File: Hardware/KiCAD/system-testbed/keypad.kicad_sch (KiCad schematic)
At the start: 43 parts, among them J6 HW-834 Module, SW10 *, SW11 2, SW12 5, SW13 8, SW14 0, SW15 3, SW16 6, SW17 9, SW18 #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

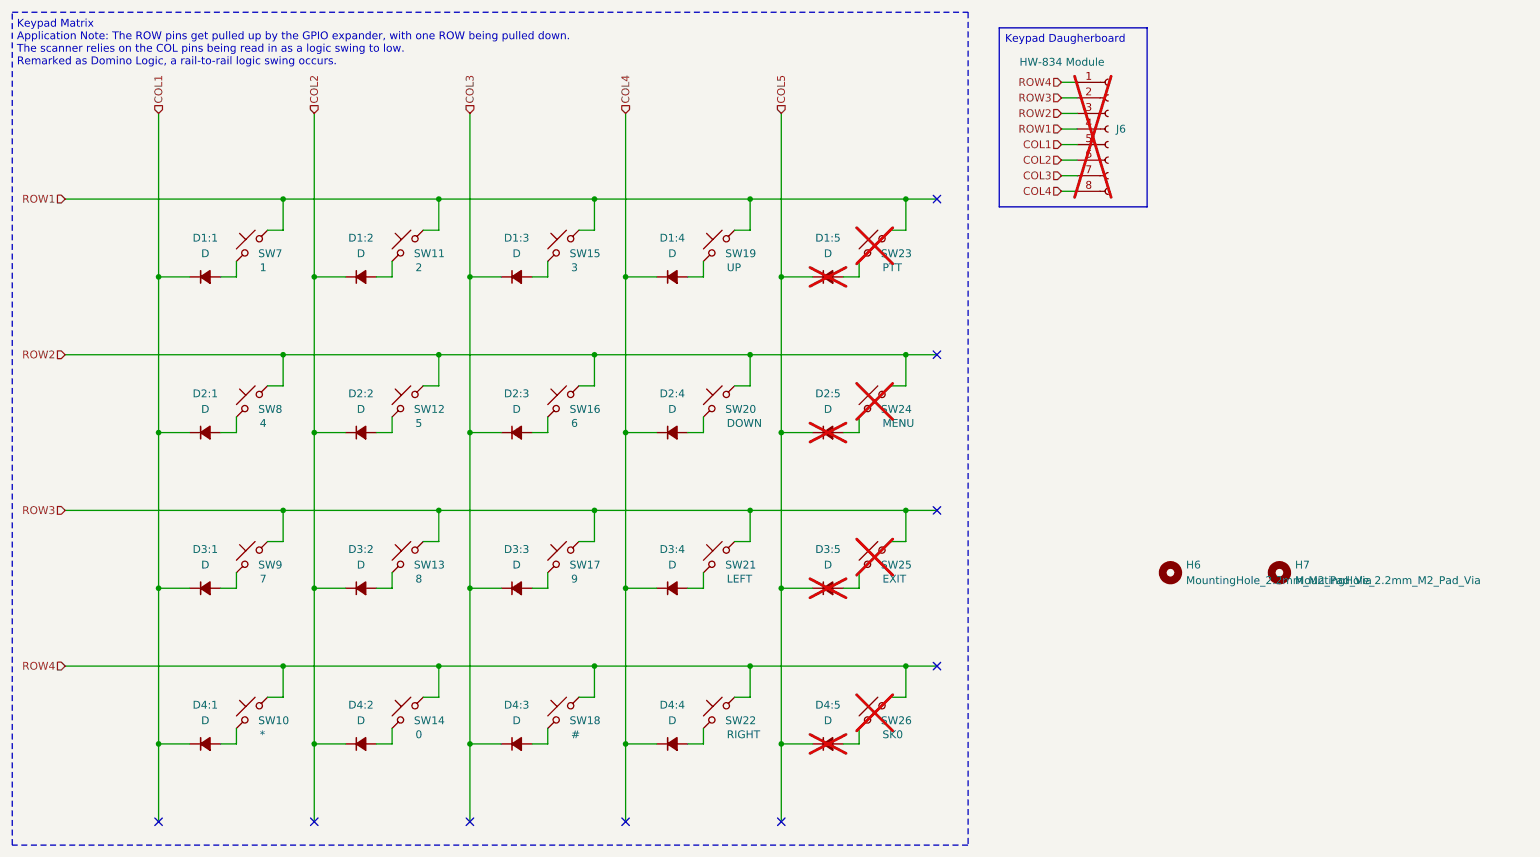
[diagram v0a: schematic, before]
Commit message: fix: remove unused mounting holes for HW #69 fix: edit symbol fields of button matrix #69
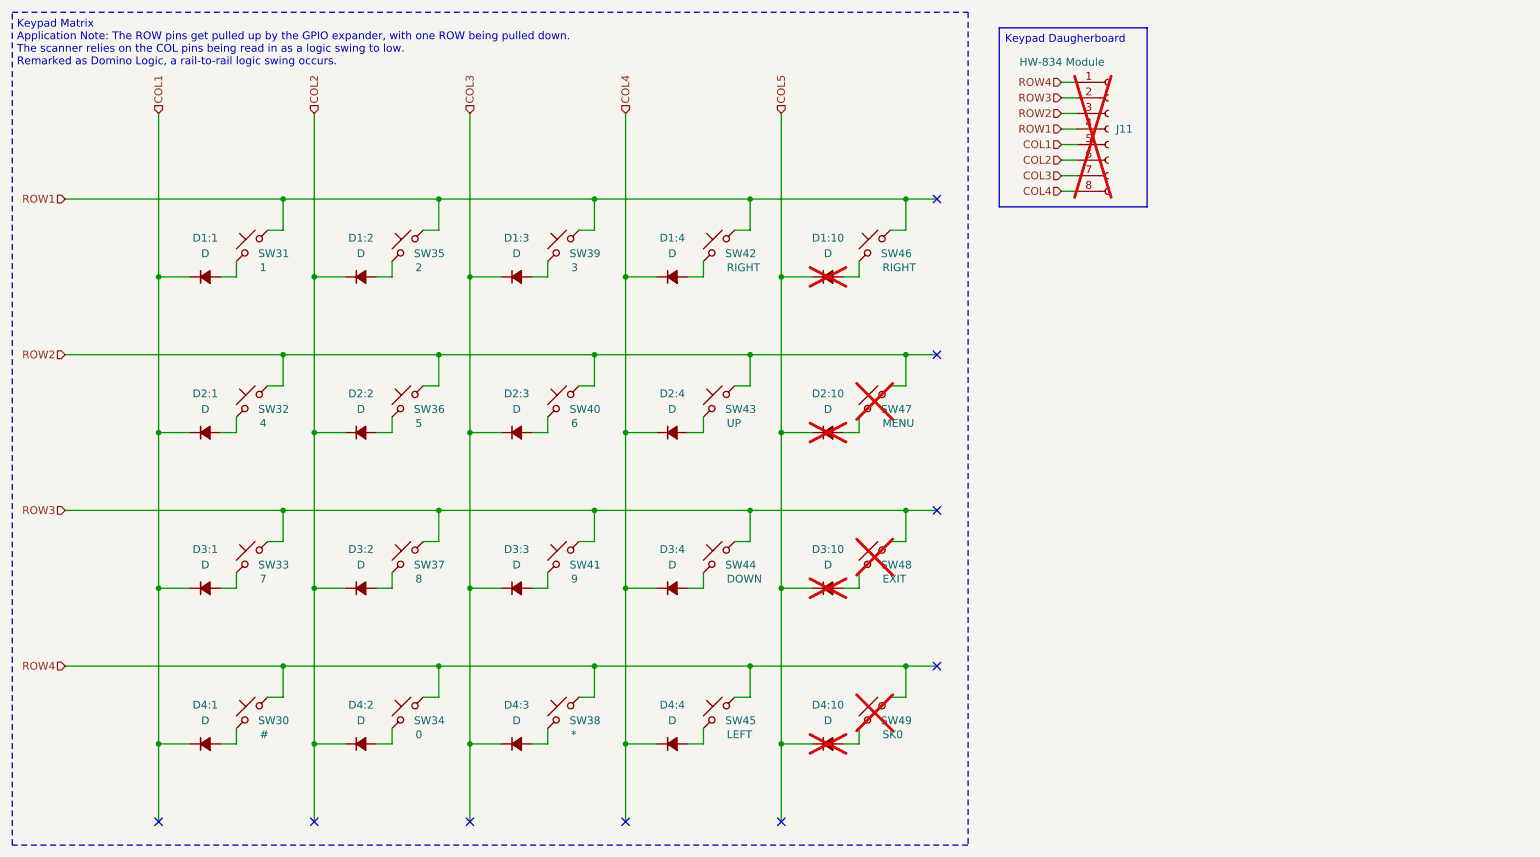
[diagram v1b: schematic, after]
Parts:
- removed H6: MountingHole_2.2mm_M2_Pad_Via, MountingHole:MountingHole_2.2mm_M2_Pad_Via, symbol Mechanical:MountingHole
- removed H7: MountingHole_2.2mm_M2_Pad_Via, MountingHole:MountingHole_6.4mm_M6_Pad_Via, symbol Mechanical:MountingHole
- SW30: renamed from SW7; value 1 -> #; footprint Button_Switch_THT:SW_PUSH_6mm_H7.3mm -> Button_Switch_SMD:SW_Push_1P1T_NO_CK_KMR2
- SW31: renamed from SW8; value 4 -> 1; footprint Button_Switch_THT:SW_PUSH_6mm_H7.3mm -> Button_Switch_SMD:SW_Push_1P1T_NO_CK_KMR2
- SW32: renamed from SW9; value 7 -> 4; footprint Button_Switch_THT:SW_PUSH_6mm_H7.3mm -> Button_Switch_SMD:SW_Push_1P1T_NO_CK_KMR2
- SW33: renamed from SW10; value * -> 7; footprint Button_Switch_THT:SW_PUSH_6mm_H7.3mm -> Button_Switch_SMD:SW_Push_1P1T_NO_CK_KMR2
- SW34: renamed from SW11; value 2 -> 0; footprint Button_Switch_THT:SW_PUSH_6mm_H7.3mm -> Button_Switch_SMD:SW_Push_1P1T_NO_CK_KMR2
- SW35: renamed from SW12; value 5 -> 2; footprint Button_Switch_THT:SW_PUSH_6mm_H7.3mm -> Button_Switch_SMD:SW_Push_1P1T_NO_CK_KMR2
- SW36: renamed from SW13; value 8 -> 5; footprint Button_Switch_THT:SW_PUSH_6mm_H7.3mm -> Button_Switch_SMD:SW_Push_1P1T_NO_CK_KMR2
- SW37: renamed from SW14; value 0 -> 8; footprint Button_Switch_THT:SW_PUSH_6mm_H7.3mm -> Button_Switch_SMD:SW_Push_1P1T_NO_CK_KMR2
- SW38: renamed from SW15; value 3 -> *; footprint Button_Switch_THT:SW_PUSH_6mm_H7.3mm -> Button_Switch_SMD:SW_Push_1P1T_NO_CK_KMR2
- SW39: renamed from SW16; value 6 -> 3; footprint Button_Switch_THT:SW_PUSH_6mm_H7.3mm -> Button_Switch_SMD:SW_Push_1P1T_NO_CK_KMR2
- SW40: renamed from SW17; value 9 -> 6; footprint Button_Switch_THT:SW_PUSH_6mm_H7.3mm -> Button_Switch_SMD:SW_Push_1P1T_NO_CK_KMR2
- SW41: renamed from SW18; value # -> 9; footprint Button_Switch_THT:SW_PUSH_6mm_H7.3mm -> Button_Switch_SMD:SW_Push_1P1T_NO_CK_KMR2
- SW42: renamed from SW19; value UP -> RIGHT; footprint Button_Switch_THT:SW_PUSH_6mm_H7.3mm -> Button_Switch_SMD:SW_Push_1P1T_NO_CK_KMR2
- SW43: renamed from SW20; value DOWN -> UP; footprint Button_Switch_THT:SW_PUSH_6mm_H7.3mm -> Button_Switch_SMD:SW_Push_1P1T_NO_CK_KMR2
- SW44: renamed from SW21; value LEFT -> DOWN; footprint Button_Switch_THT:SW_PUSH_6mm_H7.3mm -> Button_Switch_SMD:SW_Push_1P1T_NO_CK_KMR2
- SW45: renamed from SW22; value RIGHT -> LEFT; footprint Button_Switch_THT:SW_PUSH_6mm_H7.3mm -> Button_Switch_SMD:SW_Push_1P1T_NO_CK_KMR2
- SW46: renamed from SW23; value PTT -> RIGHT; footprint Button_Switch_THT:SW_PUSH_6mm_H7.3mm -> Button_Switch_SMD:SW_Push_1P1T_NO_CK_KMR2; now fitted; now in the parts list
- SW47: renamed from SW24; footprint Button_Switch_THT:SW_PUSH_6mm_H7.3mm -> Button_Switch_SMD:SW_Push_1P1T_NO_CK_KMR2
- SW48: renamed from SW25; footprint Button_Switch_THT:SW_PUSH_6mm_H7.3mm -> Button_Switch_SMD:SW_Push_1P1T_NO_CK_KMR2
- SW49: renamed from SW26; footprint Button_Switch_THT:SW_PUSH_6mm_H7.3mm -> Button_Switch_SMD:SW_Push_1P1T_NO_CK_KMR2
- renumbered D1:5 to D1:10, D2:5 to D2:10, D3:5 to D3:10, D4:5 to D4:10, J6 to J11
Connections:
- net ROW1: now also SW31.2, SW35.2, SW39.2; no longer SW30.2, SW34.2, SW38.2
- net ROW2: now also SW32.2, SW36.2, SW40.2; no longer SW31.2, SW35.2, SW39.2
- net ROW3: now also SW33.2, SW37.2, SW41.2; no longer SW32.2, SW36.2, SW40.2
- net ROW4: now also SW30.2, SW34.2, SW38.2; no longer SW33.2, SW37.2, SW41.2
- net at SW34.1: now also D4:2.2 (A); no longer D1:2.2 (A)
- net at D3:1.2 (A): now also SW33.1; no longer SW32.1
- net at SW40.1: now also D2:3.2 (A); no longer D3:3.2 (A)
- net at SW30.1: now also D4:1.2 (A); no longer D1:1.2 (A)
- net at SW38.1: now also D4:3.2 (A); no longer D1:3.2 (A)
- net at SW36.1: now also D2:2.2 (A); no longer D3:2.2 (A)
- net at D2:1.2 (A): now also SW32.1; no longer SW31.1
- net at SW41.1: now also D3:3.2 (A); no longer D4:3.2 (A)
- net at SW35.1: now also D1:2.2 (A); no longer D2:2.2 (A)
- net at SW39.1: now also D1:3.2 (A); no longer D2:3.2 (A)
- net at SW37.1: now also D3:2.2 (A); no longer D4:2.2 (A)
- new net: D1:1.2 (A), SW31.1
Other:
- moved on the sheet: SW30, SW31, SW32, SW33, SW34, SW35, SW36, SW37, SW38, SW39, SW40, SW41
